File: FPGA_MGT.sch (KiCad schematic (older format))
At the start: 47 parts, among them U1 XC7A200T-FBG484

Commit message: DDR terminations changed, HTML BoM with variant added
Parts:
- C292, C294, C314, C315, C316, C317, C318, C319, C320, C321, C322, C323, C324, C325, C326, C327, C328, C329: config (none) -> -standalone
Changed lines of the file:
@@
-EESchema Schematic File Version 5
+EESchema Schematic File Version 4
 LIBS:AMC_FMC_Carrier-PcbDoc-cache
 EELAYER 29 0
@@
 F 39 "Capacitors SMD" H 3500 770 60  0001 L CNN "Library Name"
 F 40 "This work is licensed under the Creative Commons CC-BY-SA 4.0 License. To the extent that circuit schematics that use Licensed Material can be considered to be ‘Adapted Material’, then the copyright holder waives article 3.b of the license with respect to these schematics." H 3500 680 60  0001 L CNN "License"
+F 41 "-standalone" H 3500 4450 50  0001 C CNN "config"
 	1    3500 4450
 	-1   0    0    1
@@
 F 39 "Capacitors SMD" H 3500 1270 60  0001 L CNN "Library Name"
 F 40 "This work is licensed under the Creative Commons CC-BY-SA 4.0 License. To the extent that circuit schematics that use Licensed Material can be considered to be ‘Adapted Material’, then the copyright holder waives article 3.b of the license with respect to these schematics." H 3500 1180 60  0001 L CNN "License"
+F 41 "-standalone" H 3500 4950 50  0001 C CNN "config"
 	1    3500 4950
 	-1   0    0    1
@@
 F 39 "Capacitors SMD" H 6400 -2830 60  0001 L CNN "Library Name"
 F 40 "This work is licensed under the Creative Commons CC-BY-SA 4.0 License. To the extent that circuit schematics that use Licensed Material can be considered to be ‘Adapted Material’, then the copyright holder waives article 3.b of the license with respect to these schematics." H 6400 -2920 60  0001 L CNN "License"
+F 41 "-standalone" H 6400 850 50  0001 C CNN "config"
 	1    6400 850
 	-1   0    0    1
@@
 F 39 "Capacitors SMD" H 6400 -2580 60  0001 L CNN "Library Name"
 F 40 "This work is licensed under the Creative Commons CC-BY-SA 4.0 License. To the extent that circuit schematics that use Licensed Material can be considered to be ‘Adapted Material’, then the copyright holder waives article 3.b of the license with respect to these schematics." H 6400 -2670 60  0001 L CNN "License"
+F 41 "-standalone" H 6400 1100 50  0001 C CNN "config"
 	1    6400 1100
 	-1   0    0    1
@@
 F 39 "Capacitors SMD" H 6400 -2280 60  0001 L CNN "Library Name"
 F 40 "This work is licensed under the Creative Commons CC-BY-SA 4.0 License. To the extent that circuit schematics that use Licensed Material can be considered to be ‘Adapted Material’, then the copyright holder waives article 3.b of the license with respect to these schematics." H 6400 -2370 60  0001 L CNN "License"
+F 41 "-standalone" H 6400 1400 50  0001 C CNN "config"
 	1    6400 1400
 	-1   0    0    1
@@
 F 39 "Capacitors SMD" H 6400 -2030 60  0001 L CNN "Library Name"
 F 40 "This work is licensed under the Creative Commons CC-BY-SA 4.0 License. To the extent that circuit schematics that use Licensed Material can be considered to be ‘Adapted Material’, then the copyright holder waives article 3.b of the license with respect to these schematics." H 6400 -2120 60  0001 L CNN "License"
+F 41 "-standalone" H 6400 1650 50  0001 C CNN "config"
 	1    6400 1650
 	-1   0    0    1
@@
 F 39 "Capacitors SMD" H 6400 -1730 60  0001 L CNN "Library Name"
 F 40 "This work is licensed under the Creative Commons CC-BY-SA 4.0 License. To the extent that circuit schematics that use Licensed Material can be considered to be ‘Adapted Material’, then the copyright holder waives article 3.b of the license with respect to these schematics." H 6400 -1820 60  0001 L CNN "License"
+F 41 "-standalone" H 6400 1950 50  0001 C CNN "config"
 	1    6400 1950
 	-1   0    0    1
@@
 F 39 "Capacitors SMD" H 6400 -1480 60  0001 L CNN "Library Name"
 F 40 "This work is licensed under the Creative Commons CC-BY-SA 4.0 License. To the extent that circuit schematics that use Licensed Material can be considered to be ‘Adapted Material’, then the copyright holder waives article 3.b of the license with respect to these schematics." H 6400 -1570 60  0001 L CNN "License"
+F 41 "-standalone" H 6400 2200 50  0001 C CNN "config"
 	1    6400 2200
 	-1   0    0    1
@@
 F 39 "Capacitors SMD" H 6400 -1180 60  0001 L CNN "Library Name"
 F 40 "This work is licensed under the Creative Commons CC-BY-SA 4.0 License. To the extent that circuit schematics that use Licensed Material can be considered to be ‘Adapted Material’, then the copyright holder waives article 3.b of the license with respect to these schematics." H 6400 -1270 60  0001 L CNN "License"
+F 41 "-standalone" H 6400 2500 50  0001 C CNN "config"
 	1    6400 2500
 	-1   0    0    1
@@
 F 39 "Capacitors SMD" H 6400 -930 60  0001 L CNN "Library Name"
 F 40 "This work is licensed under the Creative Commons CC-BY-SA 4.0 License. To the extent that circuit schematics that use Licensed Material can be considered to be ‘Adapted Material’, then the copyright holder waives article 3.b of the license with respect to these schematics." H 6400 -1020 60  0001 L CNN "License"
+F 41 "-standalone" H 6400 2750 50  0001 C CNN "config"
 	1    6400 2750
 	-1   0    0    1
@@
 F 39 "Capacitors SMD" H 6400 -480 60  0001 L CNN "Library Name"
 F 40 "This work is licensed under the Creative Commons CC-BY-SA 4.0 License. To the extent that circuit schematics that use Licensed Material can be considered to be ‘Adapted Material’, then the copyright holder waives article 3.b of the license with respect to these schematics." H 6400 -570 60  0001 L CNN "License"
+F 41 "-standalone" H 6400 3200 50  0001 C CNN "config"
 	1    6400 3200
 	-1   0    0    1
@@
 F 39 "Capacitors SMD" H 6400 -230 60  0001 L CNN "Library Name"
 F 40 "This work is licensed under the Creative Commons CC-BY-SA 4.0 License. To the extent that circuit schematics that use Licensed Material can be considered to be ‘Adapted Material’, then the copyright holder waives article 3.b of the license with respect to these schematics." H 6400 -320 60  0001 L CNN "License"
+F 41 "-standalone" H 6400 3450 50  0001 C CNN "config"
 	1    6400 3450
 	-1   0    0    1
@@
 F 39 "Capacitors SMD" H 6400 70  60  0001 L CNN "Library Name"
 F 40 "This work is licensed under the Creative Commons CC-BY-SA 4.0 License. To the extent that circuit schematics that use Licensed Material can be considered to be ‘Adapted Material’, then the copyright holder waives article 3.b of the license with respect to these schematics." H 6400 -20 60  0001 L CNN "License"
+F 41 "-standalone" H 6400 3750 50  0001 C CNN "config"
 	1    6400 3750
 	-1   0    0    1
@@
 F 39 "Capacitors SMD" H 6400 320 60  0001 L CNN "Library Name"
 F 40 "This work is licensed under the Creative Commons CC-BY-SA 4.0 License. To the extent that circuit schematics that use Licensed Material can be considered to be ‘Adapted Material’, then the copyright holder waives article 3.b of the license with respect to these schematics." H 6400 230 60  0001 L CNN "License"
+F 41 "-standalone" H 6400 4000 50  0001 C CNN "config"
 	1    6400 4000
 	-1   0    0    1
@@
 F 39 "Capacitors SMD" H 6400 620 60  0001 L CNN "Library Name"
 F 40 "This work is licensed under the Creative Commons CC-BY-SA 4.0 License. To the extent that circuit schematics that use Licensed Material can be considered to be ‘Adapted Material’, then the copyright holder waives article 3.b of the license with respect to these schematics." H 6400 530 60  0001 L CNN "License"
+F 41 "-standalone" H 6400 4300 50  0001 C CNN "config"
 	1    6400 4300
 	-1   0    0    1
@@
 F 39 "Capacitors SMD" H 6400 870 60  0001 L CNN "Library Name"
 F 40 "This work is licensed under the Creative Commons CC-BY-SA 4.0 License. To the extent that circuit schematics that use Licensed Material can be considered to be ‘Adapted Material’, then the copyright holder waives article 3.b of the license with respect to these schematics." H 6400 780 60  0001 L CNN "License"
+F 41 "-standalone" H 6400 4550 50  0001 C CNN "config"
 	1    6400 4550
 	-1   0    0    1
@@
 F 39 "Capacitors SMD" H 6400 1170 60  0001 L CNN "Library Name"
 F 40 "This work is licensed under the Creative Commons CC-BY-SA 4.0 License. To the extent that circuit schematics that use Licensed Material can be considered to be ‘Adapted Material’, then the copyright holder waives article 3.b of the license with respect to these schematics." H 6400 1080 60  0001 L CNN "License"
+F 41 "-standalone" H 6400 4850 50  0001 C CNN "config"
 	1    6400 4850
 	-1   0    0    1
@@
 F 39 "Capacitors SMD" H 6400 1420 60  0001 L CNN "Library Name"
 F 40 "This work is licensed under the Creative Commons CC-BY-SA 4.0 License. To the extent that circuit schematics that use Licensed Material can be considered to be ‘Adapted Material’, then the copyright holder waives article 3.b of the license with respect to these schematics." H 6400 1330 60  0001 L CNN "License"
+F 41 "-standalone" H 6400 5100 50  0001 C CNN "config"
 	1    6400 5100
 	-1   0    0    1

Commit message: BOM updated, 25MHz clock level fixed
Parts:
- U1: symbol AMC_FMC_Carrier-PcbDoc-rescue:XC7A200T-FBG484-FPGA_Xilinx_Artix7 -> AMC_FMC_Carrier-PcbDoc-rescue:XC7A200T-FBG484-FPGA_Xilinx_Artix7-AMC_FMC_Carrier-PcbDoc-rescue
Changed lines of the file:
@@
 	8850 3300 9700 3300
 $Comp
-L AMC_FMC_Carrier-PcbDoc-rescue:XC7A200T-FBG484-FPGA_Xilinx_Artix7 U?
+L AMC_FMC_Carrier-PcbDoc-rescue:XC7A200T-FBG484-FPGA_Xilinx_Artix7-AMC_FMC_Carrier-PcbDoc-rescue U?
 U 4 1 5E1BB549
 P 2100 2150

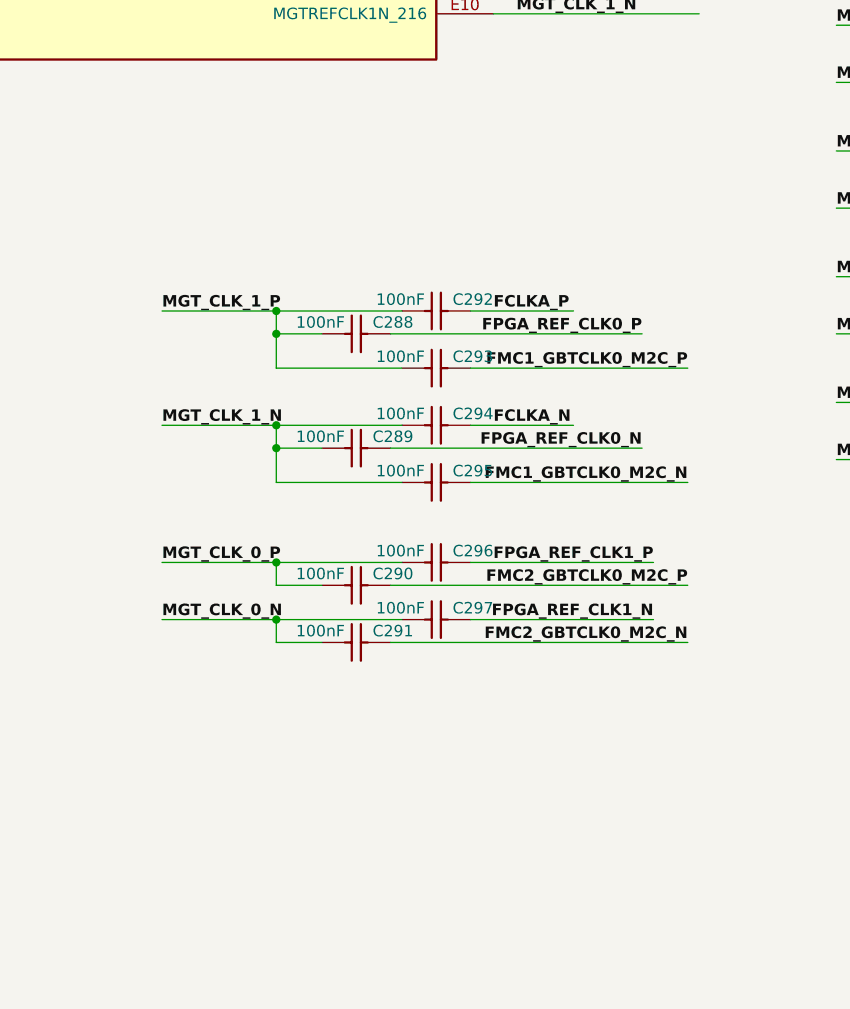
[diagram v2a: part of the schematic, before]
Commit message: U.FL for clock, logos moved, MII -> RGMII, new symbol library, git tag added
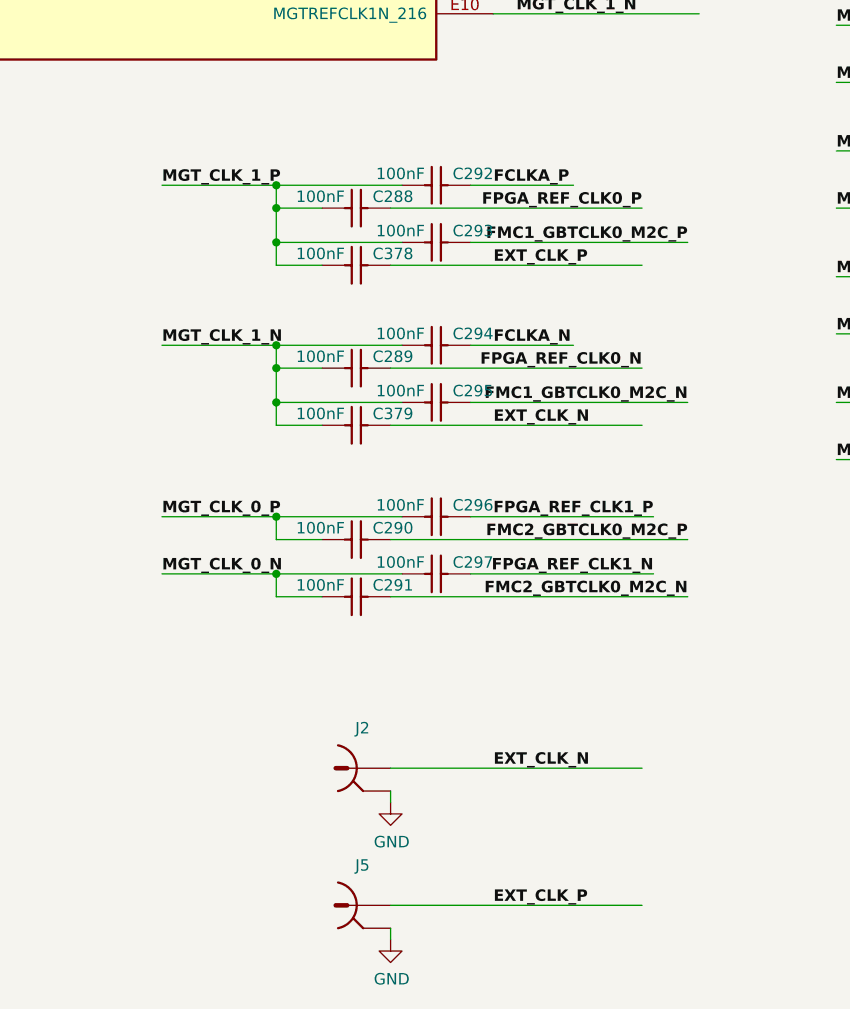
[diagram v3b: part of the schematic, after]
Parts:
- added C378, C379: CC0201_100NF_6.3V_10%_X5R, CAPC0603X33N, symbol Capacitors_SMD:CC0201_100NF_6.3V_10%_X5R
- added J2, J5: HIROSE_U.FL-R-SMT-1(10), AG5300_2:U.FL_Hirose_U.FL-R-SMT-1_Vertical, symbol Miscellaneous:HIROSE_U.FL-R-SMT-1(10)
- C288, C289, C290, C291, C293: config (none) -> dnf
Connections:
- net labels added: EXT_CLK_N, EXT_CLK_P
- wire segments 194 -> 204
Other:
- moved on the sheet: C288, C289, C290, C291, C292, C293, C294, C295, C296, C297

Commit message: more designators are visible
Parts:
- C295: config (none) -> dnf
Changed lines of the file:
@@
 $Descr A4 11693 8268
 encoding utf-8
-Sheet 19 25
+Sheet 18 25
 Title "Marble"
 Date "2019-01-16"
@@
 F 39 "Capacitors SMD" H 3500 1170 60  0001 L CNN "Library Name"
 F 40 "This work is licensed under the Creative Commons CC-BY-SA 4.0 License. To the extent that circuit schematics that use Licensed Material can be considered to be ‘Adapted Material’, then the copyright holder waives article 3.b of the license with respect to these schematics." H 3500 1080 60  0001 L CNN "License"
+F 41 "dnf" H 3500 4850 50  0001 C CNN "config"
 	1    3500 4850
 	-1   0    0    1

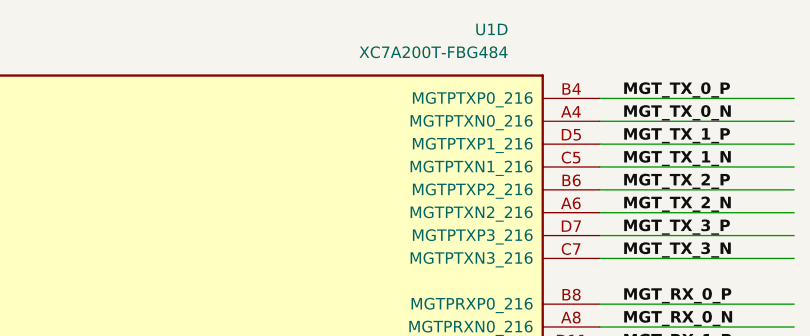
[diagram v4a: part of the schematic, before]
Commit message: BOM configuration file edited, updated Marble picture, some components part number changed
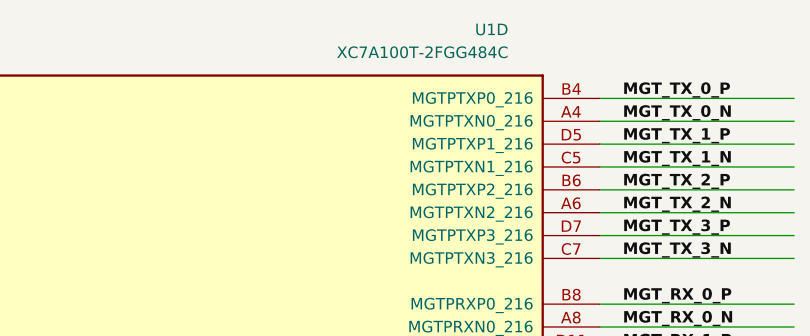
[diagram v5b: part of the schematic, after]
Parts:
- U1: value XC7A200T-FBG484 -> XC7A100T-2FGG484C; Manufacturer Part Number (none) -> XC7A100T-2FGG484C
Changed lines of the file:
@@
 AR Path="/5C907554/5DCA928C/5E1BB549" Ref="U1"  Part="4"
 F 0 "U1" H 1000 3550 50  0000 L CNN
-F 1 "XC7A200T-FBG484" H 1000 3450 50  0000 L CNN
+F 1 "XC7A100T-2FGG484C" H 1000 3450 50  0000 L CNN
 F 2 "ICs And Semiconductors SMD_BGA:BGA484C100P22X22_2300X2300X240" H 2100 2150 50  0001 C CNN
 F 3 "" H 2100 2150 50  0000 C CNN
+F 4 "XC7A100T-2FGG484C" H 2100 2150 50  0001 C CNN "Manufacturer Part Number"
 	4    2100 2150
 	-1   0    0    -1

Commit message: Rename library AMC_FMC_Carrier-PcbDoc-rescue as marble_misc
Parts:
- U1: symbol AMC_FMC_Carrier-PcbDoc-rescue:XC7A200T-FBG484-FPGA_Xilinx_Artix7-AMC_FMC_Carrier-PcbDoc-rescue -> marble_misc:XC7A200T-FBG484-FPGA_Xilinx_Artix7-AMC_FMC_Carrier-PcbDoc-rescue
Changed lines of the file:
@@
 	8850 3300 9700 3300
 $Comp
-L AMC_FMC_Carrier-PcbDoc-rescue:XC7A200T-FBG484-FPGA_Xilinx_Artix7-AMC_FMC_Carrier-PcbDoc-rescue U?
+L marble_misc:XC7A200T-FBG484-FPGA_Xilinx_Artix7-AMC_FMC_Carrier-PcbDoc-rescue U?
 U 4 1 5E1BB549
 P 2100 2150

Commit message: Strip extraneous AMC_FMC_Carrier-PcbDoc-rescue and powerMG from symbol names
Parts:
- U1: symbol marble_misc:XC7A200T-FBG484-FPGA_Xilinx_Artix7-AMC_FMC_Carrier-PcbDoc-rescue -> marble_misc:XC7A200T-FBG484-FPGA_Xilinx_Artix7
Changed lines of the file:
@@
 	8850 3300 9700 3300
 $Comp
-L marble_misc:XC7A200T-FBG484-FPGA_Xilinx_Artix7-AMC_FMC_Carrier-PcbDoc-rescue U?
+L marble_misc:XC7A200T-FBG484-FPGA_Xilinx_Artix7 U?
 U 4 1 5E1BB549
 P 2100 2150
